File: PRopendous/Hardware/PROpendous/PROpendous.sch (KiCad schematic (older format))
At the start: 0 parts

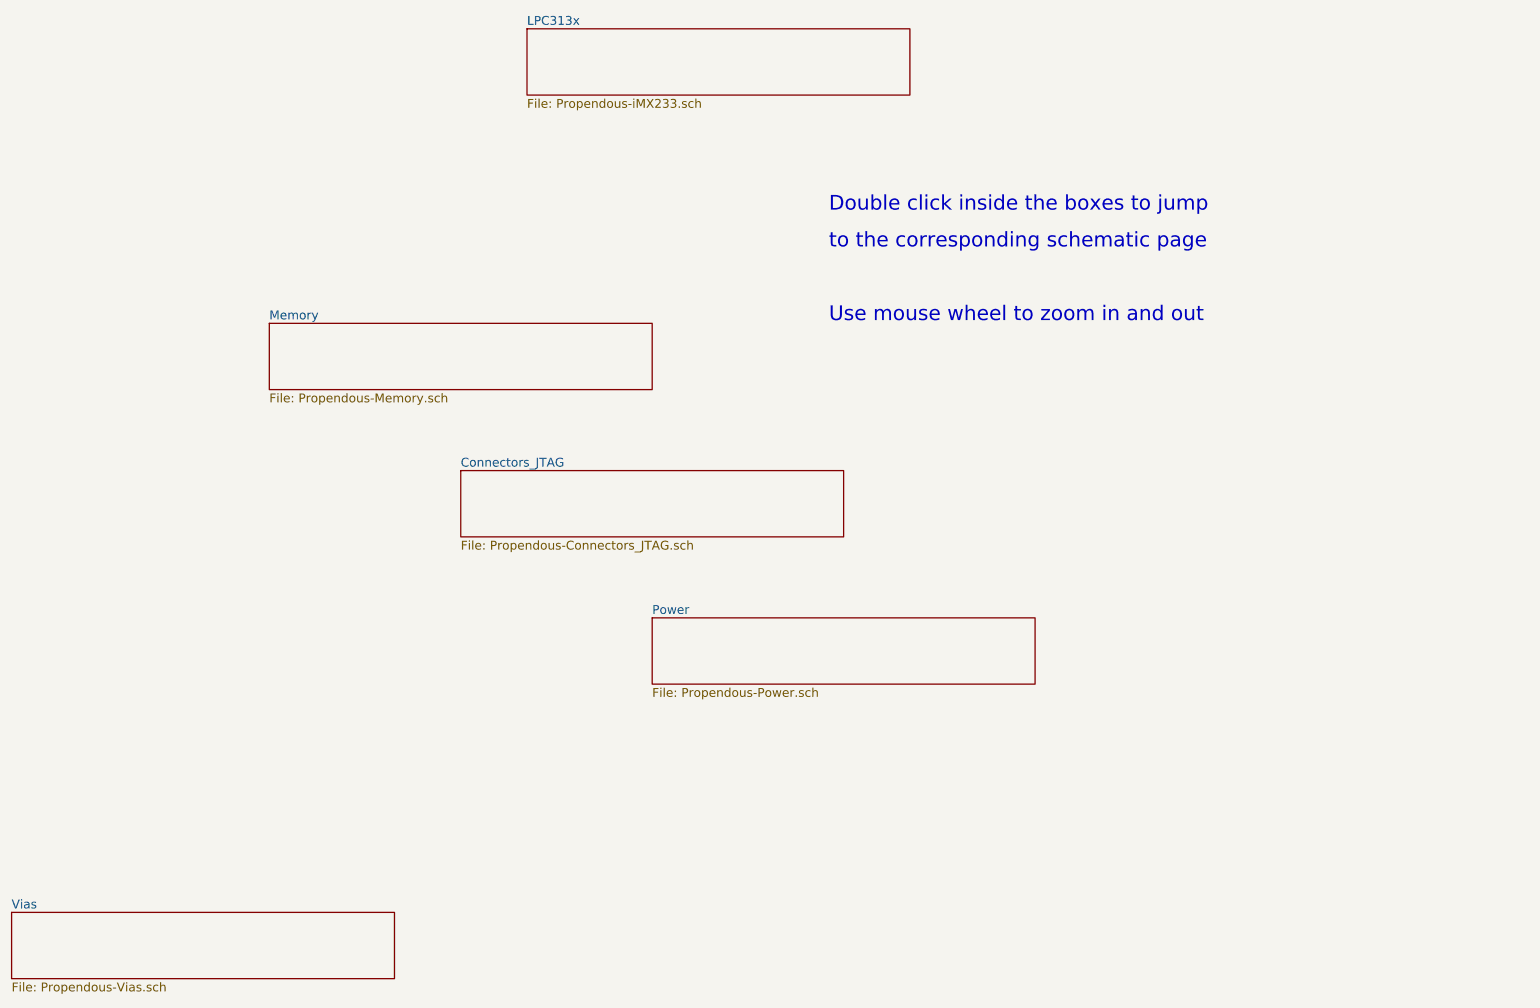
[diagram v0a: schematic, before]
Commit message: Updated files.  DDR SDRAM schematic completed.
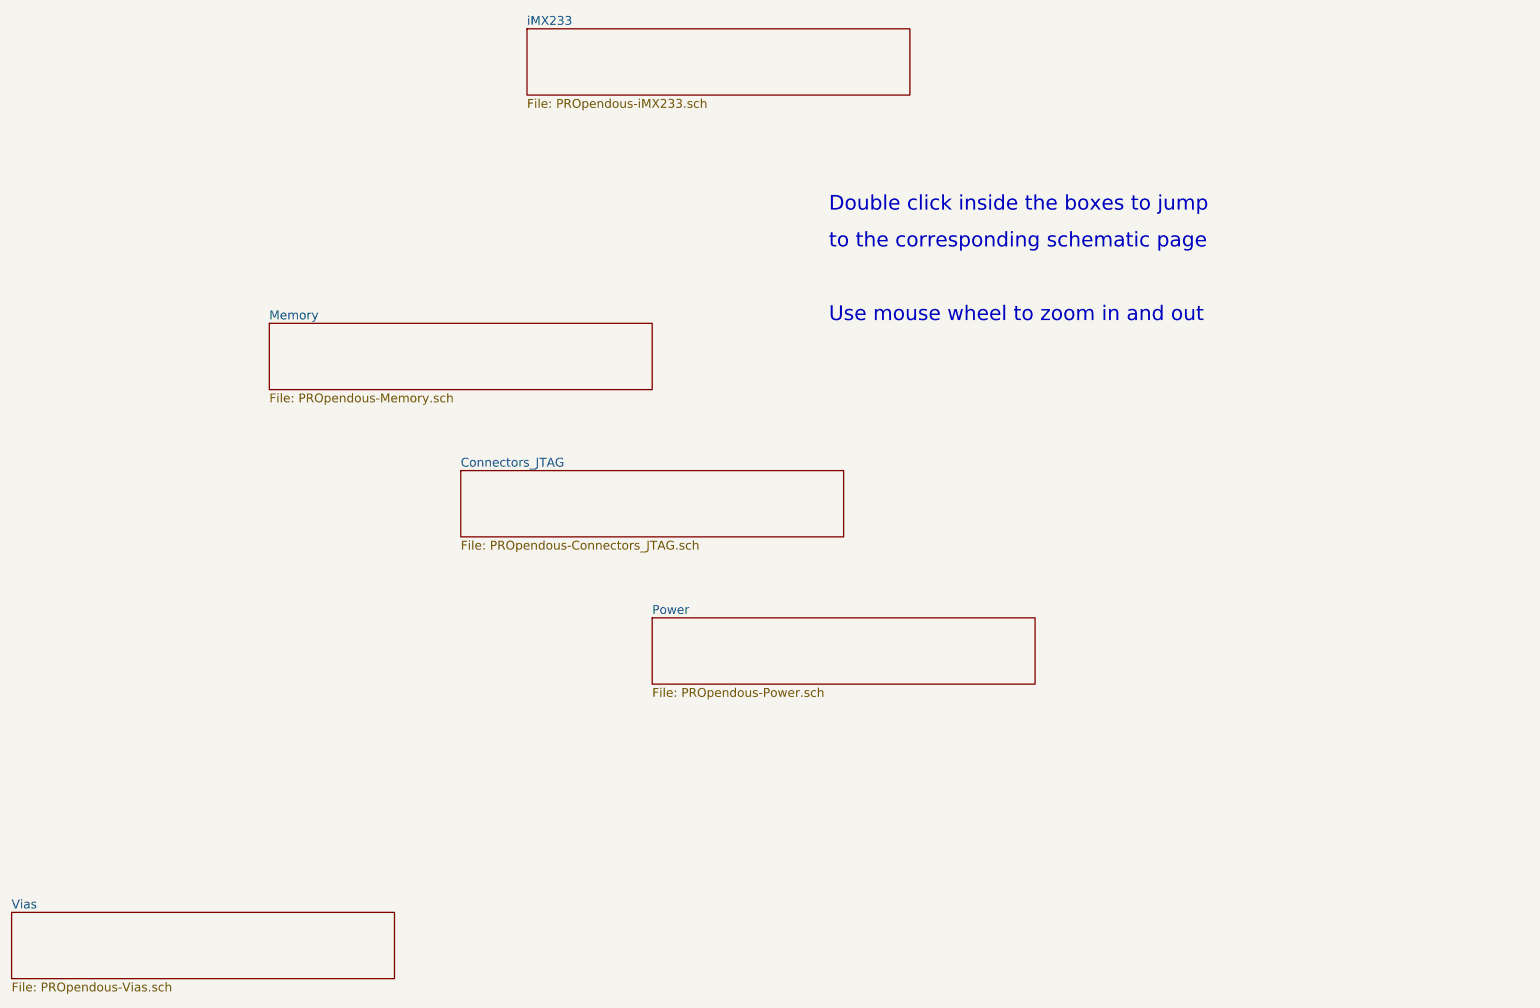
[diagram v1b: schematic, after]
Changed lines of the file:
@@
-EESchema Schematic File Version 2  date 05/04/2010 23:35:08
+EESchema Schematic File Version 2  date 07/04/2010 20:14:10
 LIBS:opendous
 LIBS:device
@@
 LIBS:valves
 LIBS:power
-LIBS:Propendous-cache
+LIBS:PROpendous-cache
 EELAYER 24  0
 EELAYER END
 $Descr A4 11700 8267
 Sheet 1 6
-Title "Propendous"
-Date "6 apr 2010"
+Title "PROpendous"
+Date "8 apr 2010"
 Rev "1.0"
 Comp "Opendous Inc. (www.opendous.org)"
@@
 Comment2 "http://creativecommons.org/licenses/by/3.0/"
 Comment3 "Copyright Under the Creative Commons Attribution License"
-Comment4 "www.Propendous.org"
+Comment4 "www.PROpendous.org"
 $EndDescr
 Text Notes 6550 3000 0    100  ~ 0
@@
 S 4500 1000 2600 450
 U 49F49153
-F0 "LPC313x" 60
-F1 "Propendous-iMX233.sch" 60
+F0 "iMX233" 60
+F1 "PROpendous-iMX233.sch" 60
 $EndSheet
 $Sheet
@@
 U 49F49538
 F0 "Memory" 60
-F1 "Propendous-Memory.sch" 60
+F1 "PROpendous-Memory.sch" 60
 $EndSheet
 $Sheet
@@
 U 49F49522
 F0 "Power" 60
-F1 "Propendous-Power.sch" 60
+F1 "PROpendous-Power.sch" 60
 $EndSheet
 $Sheet
@@
 U 49F49582
 F0 "Connectors_JTAG" 60
-F1 "Propendous-Connectors_JTAG.sch" 60
+F1 "PROpendous-Connectors_JTAG.sch" 60
 $EndSheet
 $Sheet
@@
 U 4A0869EC
 F0 "Vias" 60
-F1 "Propendous-Vias.sch" 60
+F1 "PROpendous-Vias.sch" 60
 $EndSheet
 $EndSCHEMATC

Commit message: Updated PROpendous i.MX233 project.  DDR SDRAM layout is complete.
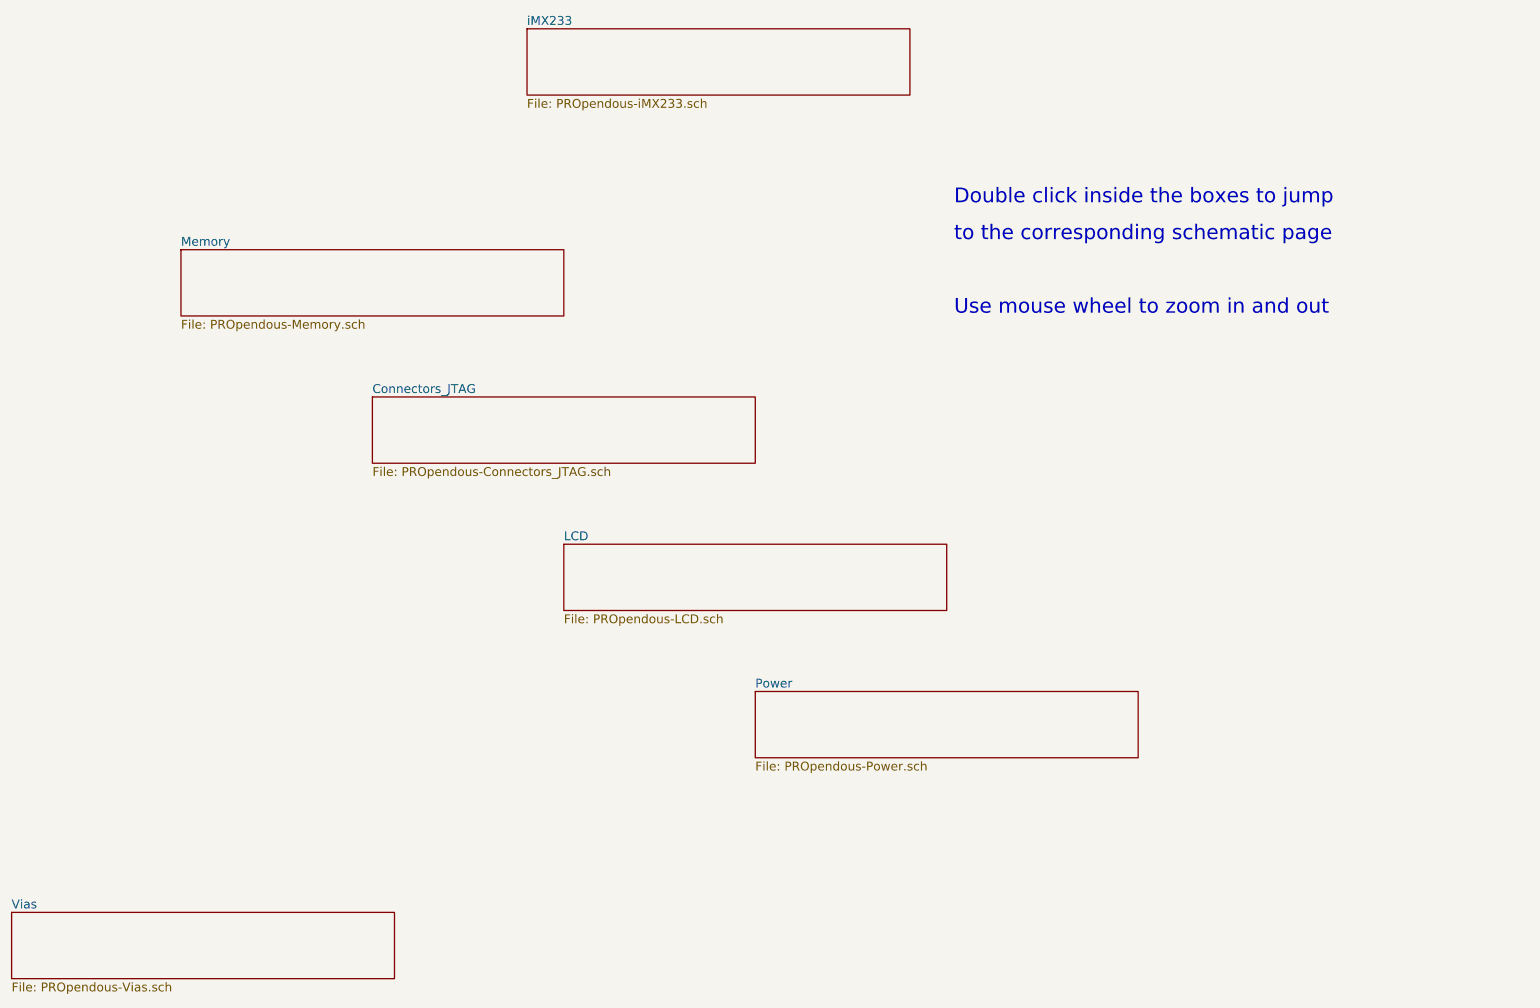
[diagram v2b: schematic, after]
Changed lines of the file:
@@
-EESchema Schematic File Version 2  date 07/04/2010 20:14:10
+EESchema Schematic File Version 2  date 17/04/2010 17:25:37
 LIBS:opendous
 LIBS:device
@@
 EELAYER END
 $Descr A4 11700 8267
-Sheet 1 6
+Sheet 1 7
 Title "PROpendous"
-Date "8 apr 2010"
+Date "17 apr 2010"
 Rev "1.0"
 Comp "Opendous Inc. (www.opendous.org)"
@@
 Comment4 "www.PROpendous.org"
 $EndDescr
-Text Notes 6550 3000 0    100  ~ 0
+Text Notes 7400 2950 0    100  ~ 0
 Use mouse wheel to zoom in and out
-Text Notes 6550 2500 0    100  ~ 0
+Text Notes 7400 2450 0    100  ~ 0
 to the corresponding schematic page
-Text Notes 6550 2250 0    100  ~ 0
+Text Notes 7400 2200 0    100  ~ 0
 Double click inside the boxes to jump
 $Sheet
@@
 $EndSheet
 $Sheet
-S 2750 3000 2600 450
+S 2150 2500 2600 450
 U 49F49538
 F0 "Memory" 60
@@
 $EndSheet
 $Sheet
-S 5350 5000 2600 450
+S 4750 4500 2600 450
 U 49F49522
-F0 "Power" 60
-F1 "PROpendous-Power.sch" 60
+F0 "LCD" 60
+F1 "PROpendous-LCD.sch" 60
 $EndSheet
 $Sheet
-S 4050 4000 2600 450
+S 3450 3500 2600 450
 U 49F49582
 F0 "Connectors_JTAG" 60
@@
 $EndSheet
 $Sheet
+S 6050 5500 2600 450
+U 4BC28B8C
+F0 "Power" 60
+F1 "PROpendous-Power.sch" 60
+$EndSheet
+$Sheet

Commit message: Updated PROpendous project.  Schematic is complete but not yet finalized.  Layout partially complete.
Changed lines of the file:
@@
-EESchema Schematic File Version 2  date 17/04/2010 17:25:37
+EESchema Schematic File Version 2  date 19/04/2010 19:59:31
 LIBS:opendous
 LIBS:device
@@
 EELAYER END
 $Descr A4 11700 8267
-Sheet 1 7
+Sheet 1 8
 Title "PROpendous"
-Date "17 apr 2010"
+Date "19 apr 2010"
 Rev "1.0"
 Comp "Opendous Inc. (www.opendous.org)"
@@
 Comment4 "www.PROpendous.org"
 $EndDescr
-Text Notes 7400 2950 0    100  ~ 0
+Text Notes 7750 3100 0    100  ~ 0
 Use mouse wheel to zoom in and out
-Text Notes 7400 2450 0    100  ~ 0
+Text Notes 7750 2600 0    100  ~ 0
 to the corresponding schematic page
-Text Notes 7400 2200 0    100  ~ 0
+Text Notes 7750 2350 0    100  ~ 0
 Double click inside the boxes to jump
 $Sheet
@@
 $EndSheet
 $Sheet
-S 2150 2500 2600 450
+S 1400 1850 2600 450
 U 49F49538
 F0 "Memory" 60
@@
 $EndSheet
 $Sheet
-S 4750 4500 2600 450
+S 2700 2850 2600 450
+U 49F49582
+F0 "Connectors_JTAG" 60
+F1 "PROpendous-Connectors_JTAG.sch" 60
+$EndSheet
+$Sheet
+S 4000 3850 2600 450
 U 49F49522
 F0 "LCD" 60
@@
 $EndSheet
 $Sheet
-S 3450 3500 2600 450
-U 49F49582
-F0 "Connectors_JTAG" 60
-F1 "PROpendous-Connectors_JTAG.sch" 60
+S 5300 4850 2600 450
+U 4BCC4A78
+F0 "Audio" 60
+F1 "PROpendous-Audio.sch" 60
 $EndSheet
 $Sheet
-S 6050 5500 2600 450
+S 6600 5850 2600 450
 U 4BC28B8C
-F0 "Power" 60
-F1 "PROpendous-Power.sch" 60
+F0 "Power_Boot" 60
+F1 "PROpendous-Power_Boot.sch" 60
 $EndSheet
 $Sheet
